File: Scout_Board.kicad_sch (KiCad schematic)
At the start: 3 parts, among them U1 ESP32-S3-DEVKITC-1U-N8R2

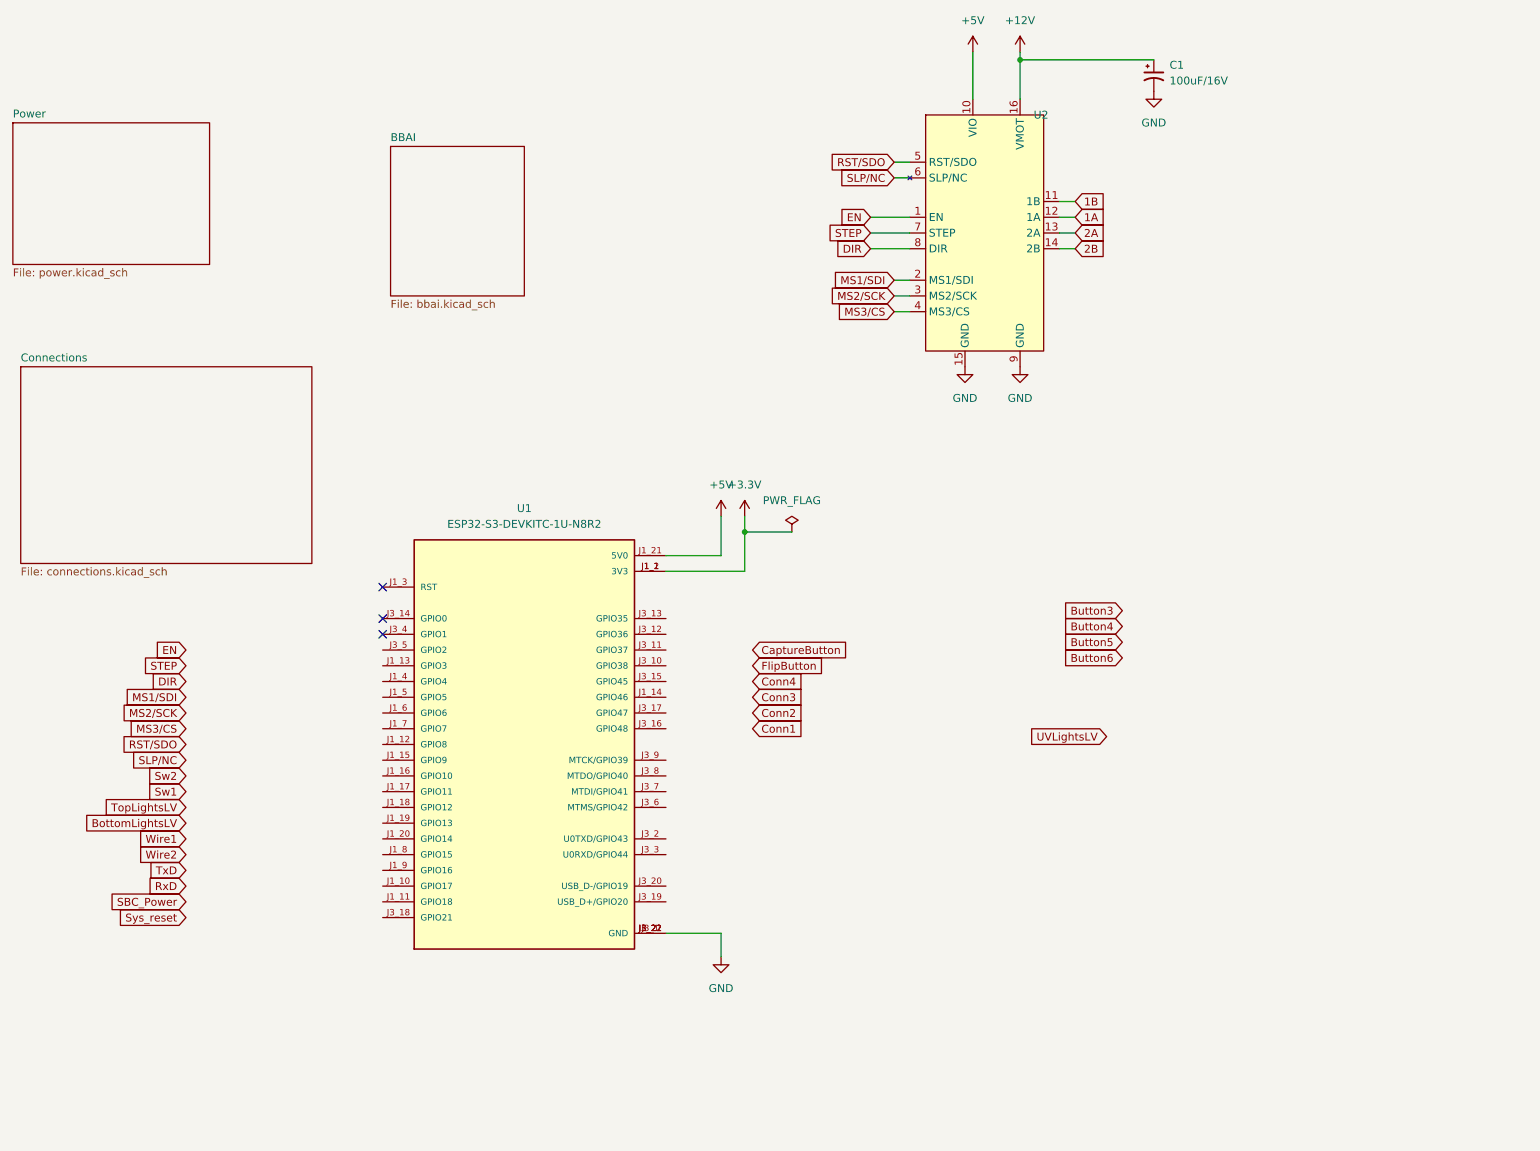
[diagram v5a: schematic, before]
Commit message: Layout updated with mounting holes
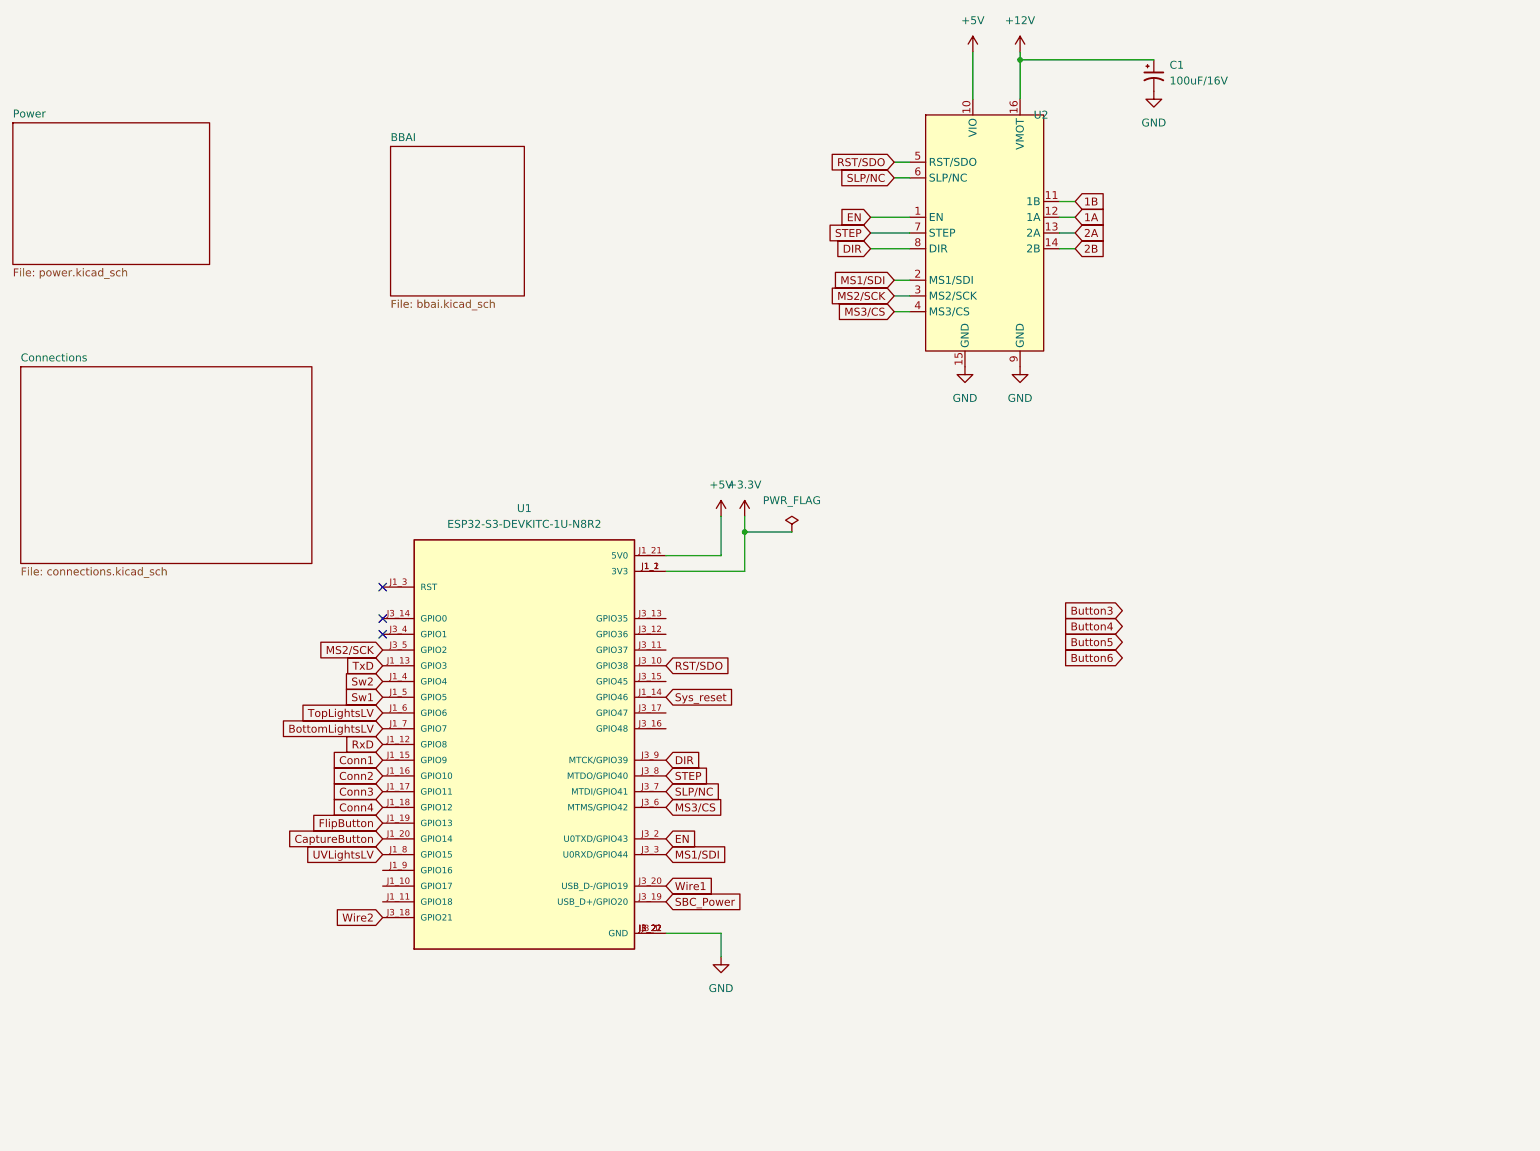
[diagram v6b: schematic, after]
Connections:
- net BottomLightsLV: now also U1.J1_7 (GPIO7)
- net CaptureButton: now also U1.J1_20 (GPIO14)
- net Conn1: now also U1.J1_15 (GPIO9)
- net Conn2: now also U1.J1_16 (GPIO10)
- net Conn3: now also U1.J1_17 (GPIO11)
- net Conn4: now also U1.J1_18 (GPIO12)
- net DIR: now also U1.J3_9 (MTCK/GPIO39)
- net EN: now also U1.J3_2 (U0TXD/GPIO43)
- net FlipButton: now also U1.J1_19 (GPIO13)
- net MS1/SDI: now also U1.J3_3 (U0RXD/GPIO44)
- net MS2/SCK: now also U1.J3_5 (GPIO2)
- net MS3/CS: now also U1.J3_6 (MTMS/GPIO42)
- net RST/SDO: now also U1.J3_10 (GPIO38)
- net RxD: now also U1.J1_12 (GPIO8)
- net SBC_Power: now also U1.J3_19 (USB_D+/GPIO20)
- net SLP/NC: now also U1.J3_7 (MTDI/GPIO41)
- net STEP: now also U1.J3_8 (MTDO/GPIO40)
- net Sw1: now also U1.J1_5 (GPIO5)
- net Sw2: now also U1.J1_4 (GPIO4)
- net Sys_reset: now also U1.J1_14 (GPIO46)
- net TopLightsLV: now also U1.J1_6 (GPIO6)
- net TxD: now also U1.J1_13 (GPIO3)
- net UVLightsLV: now also U1.J1_8 (GPIO15)
- net Wire1: now also U1.J3_20 (USB_D-/GPIO19)
- net Wire2: now also U1.J3_18 (GPIO21)

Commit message: Updated board
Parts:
- added JP1: Jumper_2_Open, TestPoint:TestPoint_2Pads_Pitch2.54mm_Drill0.8mm, symbol Jumper:Jumper_2_Open
- C1: LCSC (none) -> C111600; Part Number (none) -> 865080343009
- U2: value ~ -> Steppper motor driver
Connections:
- net Conn1: now also U1.J1_18 (GPIO12); no longer U1.J1_15 (GPIO9)
- net Conn2: now also U1.J3_18 (GPIO21); no longer U1.J1_16 (GPIO10)
- net Conn4: now also U1.J3_17 (GPIO47); no longer U1.J1_18 (GPIO12)
- net RST/SDO: now also JP1.1 (A)
- net RxD: now also U1.J1_14 (GPIO46); no longer U1.J1_12 (GPIO8)
- net SBC_Power: now also U1.J3_11 (GPIO37); no longer U1.J3_19 (USB_D+/GPIO20)
- net SLP/NC: now also JP1.2 (B)
- net Sys_reset: now also U1.J1_12 (GPIO8); no longer U1.J1_14 (GPIO46)
- net Wire1: now also U1.J3_13 (GPIO35); no longer U1.J3_20 (USB_D-/GPIO19)
- net Wire2: now also U1.J3_12 (GPIO36); no longer U1.J3_18 (GPIO21)
- net Conn8: now reaches U1.J3_15 (GPIO45)
- net Conn6: now reaches U1.J3_16 (GPIO48)
- new net Conn5: U1.J1_16 (GPIO10)
- new net Conn7: U1.J1_15 (GPIO9)
